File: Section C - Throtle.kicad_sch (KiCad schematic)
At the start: 19 parts, among them U6 74HCT125D,653, U7 LMV358, U8 LMV358

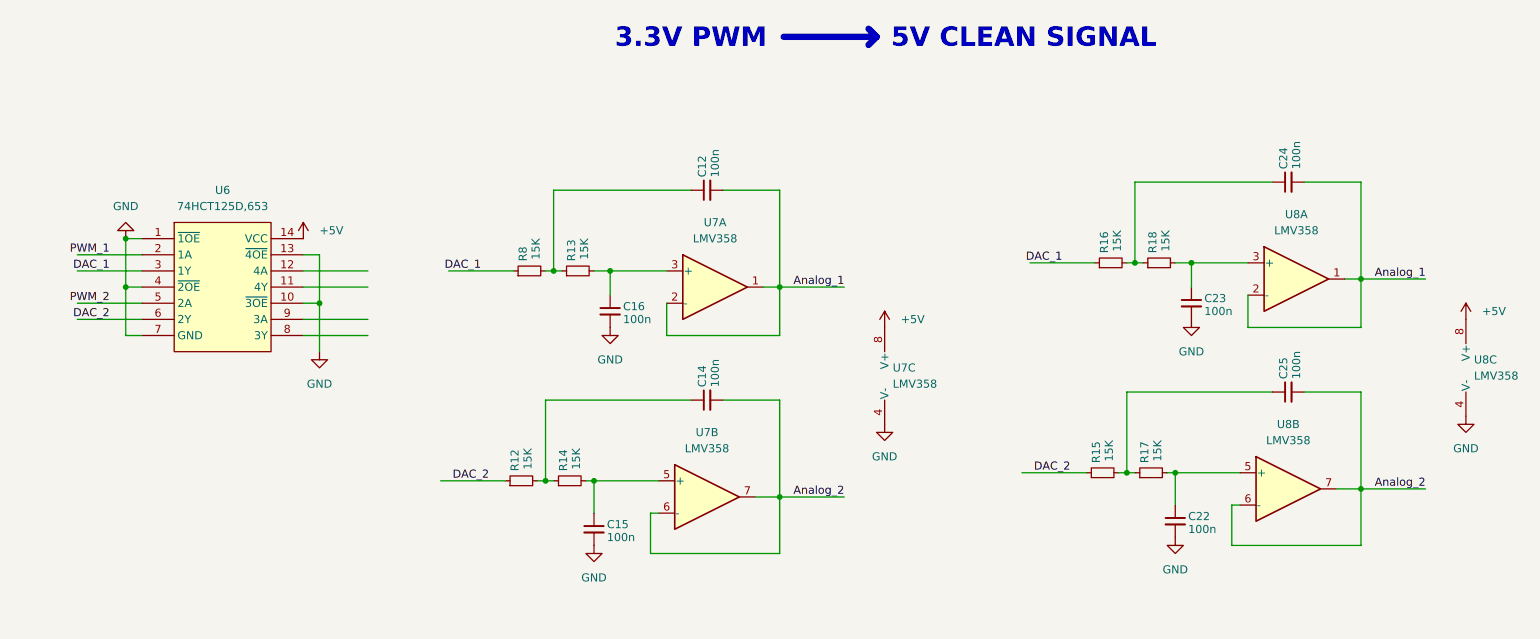
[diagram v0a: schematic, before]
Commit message: add CAN port, change power regulation
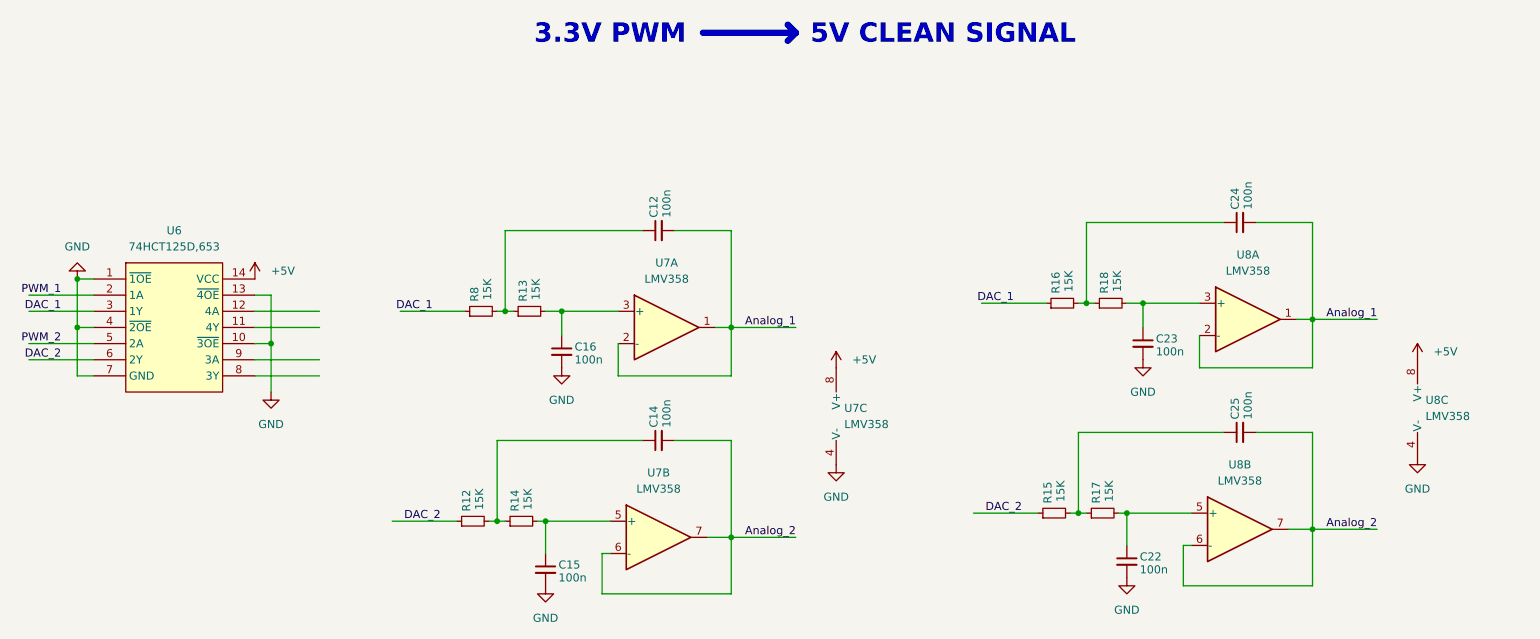
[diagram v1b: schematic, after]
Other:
- moved on the sheet: C12, C14, C15, C16, C22, C23, C24, C25, R12, R13, R14, R15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
